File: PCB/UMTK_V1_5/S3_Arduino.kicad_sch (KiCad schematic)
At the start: 30 parts

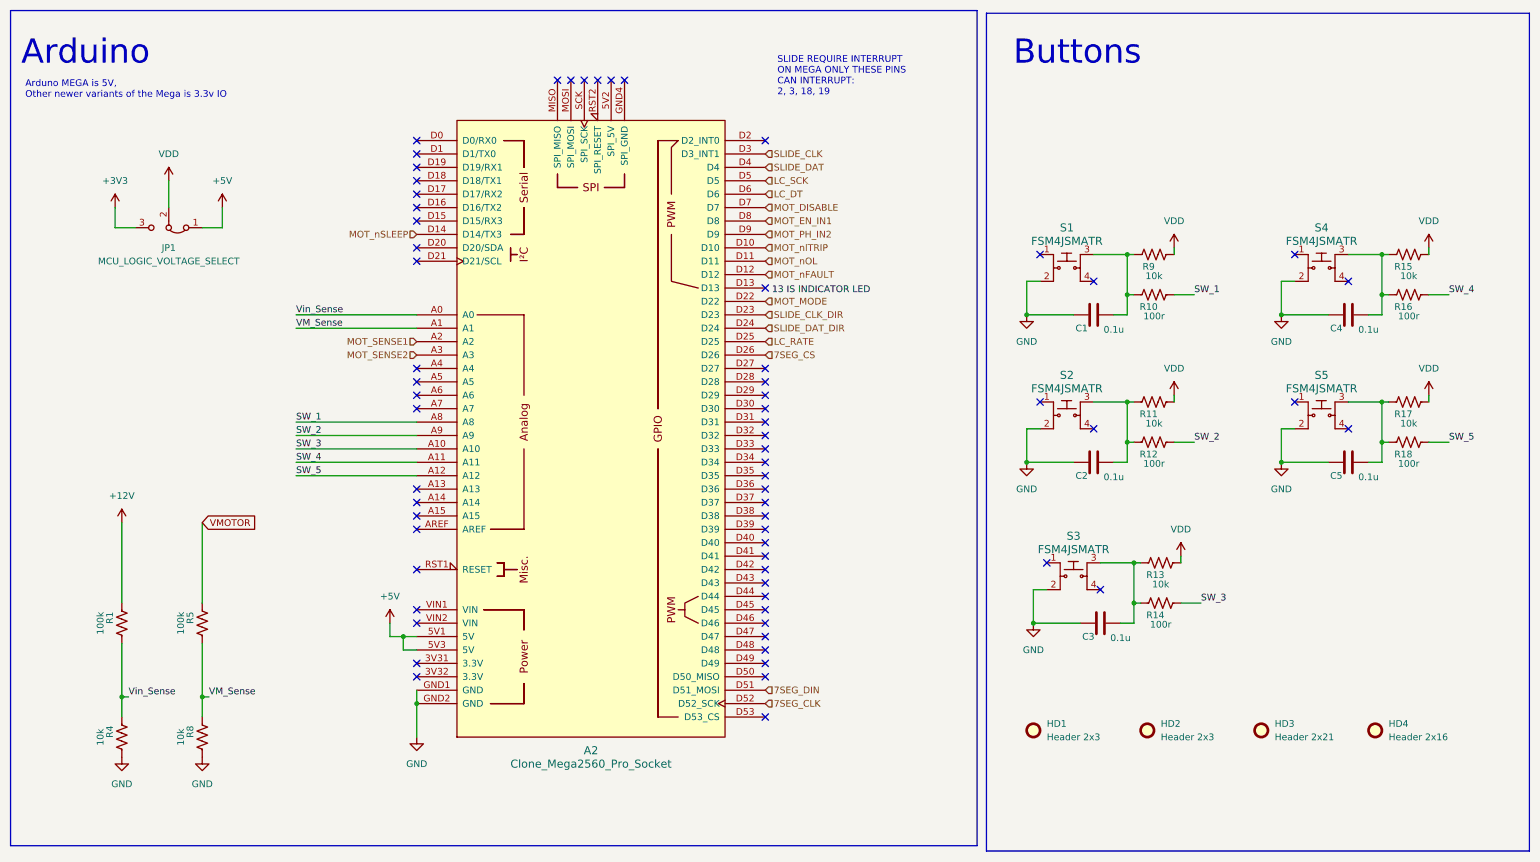
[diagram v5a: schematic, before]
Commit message: PCB Revision
- Add filter for 7seg power again
- Add low pass filter for output of motor power sense
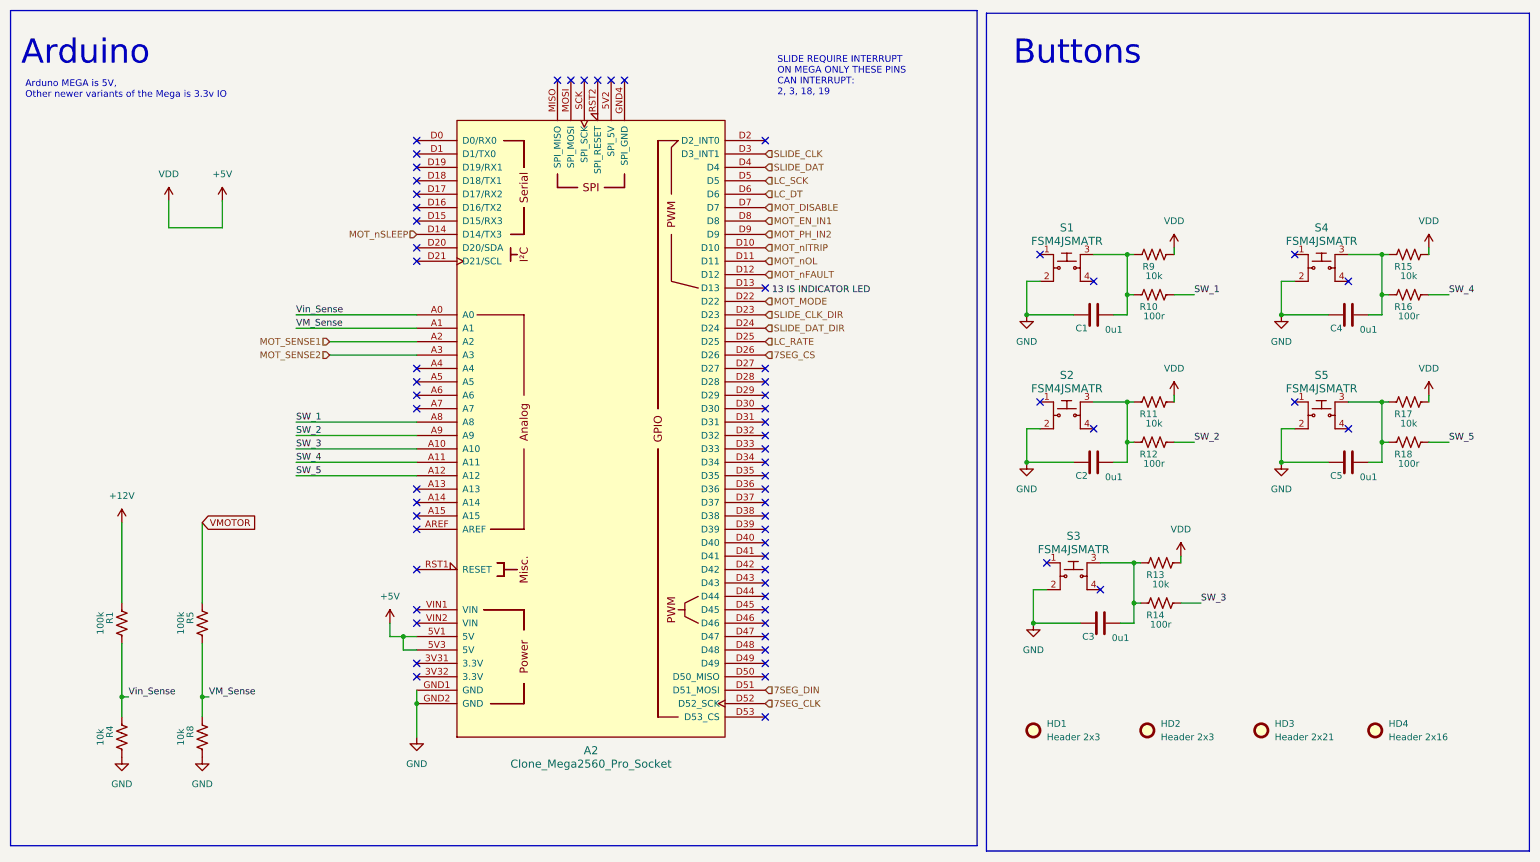
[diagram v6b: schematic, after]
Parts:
- removed JP1: MCU_LOGIC_VOLTAGE_SELECT, Jumper:SolderJumper-3_P1.3mm_Bridged12_Pad1.0x1.5mm, symbol Jumper:Jumper_3_Bridged12
- A2: footprint arduino-library:Clone_Mega2560_Pro_Socket -> AMX_Logo:Clone_Mega2560_Pro_Socket
- C1, C2, C3, C4, C5: value 0.1u -> 0u1
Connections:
- net VDD is gone; now on net +5V: R11.2, R13.2, R15.2, R17.2, R9.2
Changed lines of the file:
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@@
 	(wire
 		(pts
-			(xy 200.66 129.54) (xy 198.12 129.54)
+			(xy 64.77 85.09) (xy 81.28 85.09)
 		)
 		(stroke
@@
 	(wire
 		(pts
-			(xy 24.13 57.15) (xy 24.13 60.96)
+			(xy 200.66 129.54) (xy 198.12 129.54)
 		)
 		(stroke
@@
 	(wire
 		(pts
-			(xy 44.45 60.96) (xy 40.64 60.96)
+			(xy 264.16 93.98) (xy 265.43 93.98)
 		)
 		(stroke
@@
 	(wire
 		(pts
-			(xy 264.16 93.98) (xy 265.43 93.98)
+			(xy 34.29 60.96) (xy 34.29 55.88)
 		)
 		(stroke
@@
 	(wire
 		(pts
-			(xy 264.16 105.41) (xy 264.16 101.6)
+			(xy 64.77 82.55) (xy 81.28 82.55)
 		)
 		(stroke
@@
 	(wire
 		(pts
-			(xy 264.16 93.98) (xy 264.16 101.6)
+			(xy 264.16 105.41) (xy 264.16 101.6)
 		)
 		(stroke
@@
 	(wire
 		(pts
-			(xy 264.16 66.04) (xy 265.43 66.04)
+			(xy 264.16 93.98) (xy 264.16 101.6)
 		)
 		(stroke
@@
 	(wire
 		(pts
-			(xy 199.39 99.06) (xy 196.85 99.06)
+			(xy 264.16 66.04) (xy 265.43 66.04)
 		)
 		(stroke
@@
 	(wire
 		(pts
-			(xy 245.11 99.06) (xy 245.11 105.41)
+			(xy 199.39 99.06) (xy 196.85 99.06)
 		)
 		(stroke
@@
 	(wire
 		(pts
-			(xy 273.05 101.6) (xy 276.86 101.6)
+			(xy 245.11 99.06) (xy 245.11 105.41)
 		)
 		(stroke
@@
 	(wire
 		(pts
-			(xy 245.11 77.47) (xy 254 77.47)
+			(xy 273.05 101.6) (xy 276.86 101.6)
 		)
 		(stroke
@@
 	(wire
 		(pts
-			(xy 245.11 71.12) (xy 245.11 77.47)
+			(xy 245.11 77.47) (xy 254 77.47)
 		)
 		(stroke
@@
 	(wire
 		(pts
-			(xy 44.45 57.15) (xy 44.45 60.96)
+			(xy 245.11 71.12) (xy 245.11 77.47)
 		)
 		(stroke
@@
 	(wire
 		(pts
-			(xy 261.62 105.41) (xy 264.16 105.41)
+			(xy 44.45 60.96) (xy 34.29 60.96)
 		)
 		(stroke
@@
 	(wire
 		(pts
-			(xy 24.13 60.96) (xy 27.94 60.96)
+			(xy 44.45 55.88) (xy 44.45 60.96)
 		)
 		(stroke
@@
 	(wire
 		(pts
-			(xy 34.29 52.07) (xy 34.29 57.15)
+			(xy 261.62 105.41) (xy 264.16 105.41)
 		)
 		(stroke
@@
 	(hierarchical_label "MOT_SENSE1"
 		(shape input)
-		(at 81.28 82.55 180)
+		(at 64.77 82.55 180)
 		(fields_autoplaced yes)
 		(effects
@@
 	(hierarchical_label "MOT_SENSE2"
 		(shape input)
-		(at 81.28 85.09 180)
+		(at 64.77 85.09 180)
 		(fields_autoplaced yes)
 		(effects
@@
 			)
 		)
-		(property "Value" "0.1u"
+		(property "Value" "0u1"
 			(at 261.62 80.264 90)
 			(effects
@@
 	(symbol
 		(lib_id "power:+5V")
-		(at 44.45 57.15 0)
+		(at 44.45 55.88 0)
 		(unit 1)
 		(exclude_from_sim no)
@@
 		(fields_autoplaced yes)
 		(property "Reference" "#PWR01"
-			(at 44.45 60.96 0)
+			(at 44.45 59.69 0)
 			(effects
 				(font
@@
 		)
 		(property "Value" "+5V"
-			(at 44.45 52.07 0)
+			(at 44.45 50.8 0)
 			(effects
 				(font
@@
 		)
 		(property "Footprint" ""
-			(at 44.45 57.15 0)
+			(at 44.45 55.88 0)
 			(effects
 				(font
@@
 		)
 		(property "Datasheet" ""
-			(at 44.45 57.15 0)
+			(at 44.45 55.88 0)
 			(effects
 				(font
@@
 		)
 		(property "Description" "Power symbol creates a global label with name \"+5V\""
-			(at 44.45 57.15 0)
+			(at 44.45 55.88 0)
 			(effects
 				(font
@@
 			)
 		)
-		(property "Value" "0.1u"
+		(property "Value" "0u1"
 			(at 261.62 108.204 90)
 			(effects
@@
 			)
 		)
-		(property "Value" "0.1u"
+		(property "Value" "0u1"
 			(at 213.36 80.264 90)
 			(effects
@@
 			)
 		)
-		(property "Footprint" "arduino-library:Clone_Mega2560_Pro_Socket"
+		(property "Footprint" "AMX_Logo:Clone_Mega2560_Pro_Socket"
 			(at 114.3 172.72 0)
 			(effects
@@
 	)
 	(symbol
-		(lib_id "Jumper:Jumper_3_Bridged12")
-		(at 34.29 60.96 180)
-		(unit 1)
-		(exclude_from_sim yes)
-		(in_bom no)
-		(on_board yes)
-		(dnp no)
-		(fields_autoplaced yes)
-		(property "Reference" "JP1"
-			(at 34.29 64.77 0)
-			(effects
-				(font
-					(size 1.27 1.27)
-				)
-			)
-		)
-		(property "Value" "MCU_LOGIC_VOLTAGE_SELECT"
-			(at 34.29 67.31 0)
-			(effects
-				(font
-					(size 1.27 1.27)
-				)
-			)
-		)
-		(property "Footprint" "Jumper:SolderJumper-3_P1.3mm_Bridged12_Pad1.0x1.5mm"
-			(at 34.29 60.96 0)
-			(effects
-				(font
-					(size 1.27 1.27)
-				)
-				(hide yes)
-			)
-		)
-		(property "Datasheet" "~"
-			(at 34.29 60.96 0)
-			(effects
-				(font
-					(size 1.27 1.27)
-				)
-				(hide yes)
-			)
-		)
-		(property "Description" "Jumper, 3-pole, pins 1+2 closed/bridged"
-			(at 34.29 60.96 0)
-			(effects
-				(font
-					(size 1.27 1.27)
-				)
-				(hide yes)
-			)
-		)
-		(pin "1"
-		)
-		(pin "2"
-		)
-		(pin "3"
-		)
-		(instances
-			(project "UMTK"
-				(path "/2bf3ea67-58b8-47b3-a768-ea6950b40edf/5307a5c4-d831-4669-9d3e-75e94c372d80"
-					(reference "JP1")
-					(unit 1)
-				)
-			)
-		)
-	)
-	(symbol
 		(lib_id "dk_Tactile-Switches:FSM4JSMATR")
 		(at 204.47 68.58 0)
@@
 	)
 	(symbol
-		(lib_id "power:+3V3")
-		(at 24.13 57.15 0)
-		(unit 1)
-		(exclude_from_sim no)
-		(in_bom yes)
-		(on_board yes)
-		(dnp no)
-		(fields_autoplaced yes)
-		(property "Reference" "#PWR06"
-			(at 24.13 60.96 0)
-			(effects
-				(font
-					(size 1.27 1.27)
-				)
-				(hide yes)
-			)
-		)
-		(property "Value" "+3V3"
-			(at 24.13 52.07 0)
-			(effects
-				(font
-					(size 1.27 1.27)
-				)
-			)
-		)
-		(property "Footprint" ""
-			(at 24.13 57.15 0)
-			(effects
-				(font
-					(size 1.27 1.27)
-				)
-				(hide yes)
-			)
-		)
-		(property "Datasheet" ""
-			(at 24.13 57.15 0)
-			(effects
-				(font
-					(size 1.27 1.27)
-				)
-				(hide yes)
-			)
-		)
-		(property "Description" "Power symbol creates a global label with name \"+3V3\""
-			(at 24.13 57.15 0)
-			(effects
-				(font
-					(size 1.27 1.27)
-				)
-				(hide yes)
-			)
-		)
-		(pin "1"
-		)
-		(instances
-			(project "UMTK"
-				(path "/2bf3ea67-58b8-47b3-a768-ea6950b40edf/5307a5c4-d831-4669-9d3e-75e94c372d80"
-					(reference "#PWR06")
-					(unit 1)
-				)
-			)
-		)
-	)
-	(symbol
 		(lib_id "power:GND")
 		(at 245.11 105.41 0)
@@
 			)
 		)
-		(property "Value" "0.1u"
+		(property "Value" "0u1"
 			(at 213.36 108.204 90)
 			(effects
@@
 			)
 		)
-		(property "Value" "0.1u"
+		(property "Value" "0u1"
 			(at 214.63 138.684 90)
 			(effects
@@
 	(symbol
 		(lib_id "power:VDD")
-		(at 34.29 52.07 0)
+		(at 34.29 55.88 0)
 		(unit 1)
 		(exclude_from_sim no)
@@
 		(fields_autoplaced yes)
 		(property "Reference" "#PWR04"
-			(at 34.29 55.88 0)
+			(at 34.29 59.69 0)
 			(effects
 				(font
@@
 		)
 		(property "Value" "VDD"
-			(at 34.29 46.99 0)
+			(at 34.29 50.8 0)
 			(effects
 				(font
@@
 		)
 		(property "Footprint" ""
-			(at 34.29 52.07 0)
+			(at 34.29 55.88 0)
 			(effects
 				(font
@@
 		)
 		(property "Datasheet" ""
-			(at 34.29 52.07 0)
+			(at 34.29 55.88 0)
 			(effects
 				(font
@@
 		)
 		(property "Description" "Power symbol creates a global label with name \"VDD\""
-			(at 34.29 52.07 0)
+			(at 34.29 55.88 0)
 			(effects
 				(font
